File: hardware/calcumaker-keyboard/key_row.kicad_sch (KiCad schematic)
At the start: 30 parts, among them SW1 MX, SW10 MX, SW2 MX, SW3 MX, SW4 MX, SW5 MX, SW6 MX, SW7 MX, SW8 MX, SW9 MX

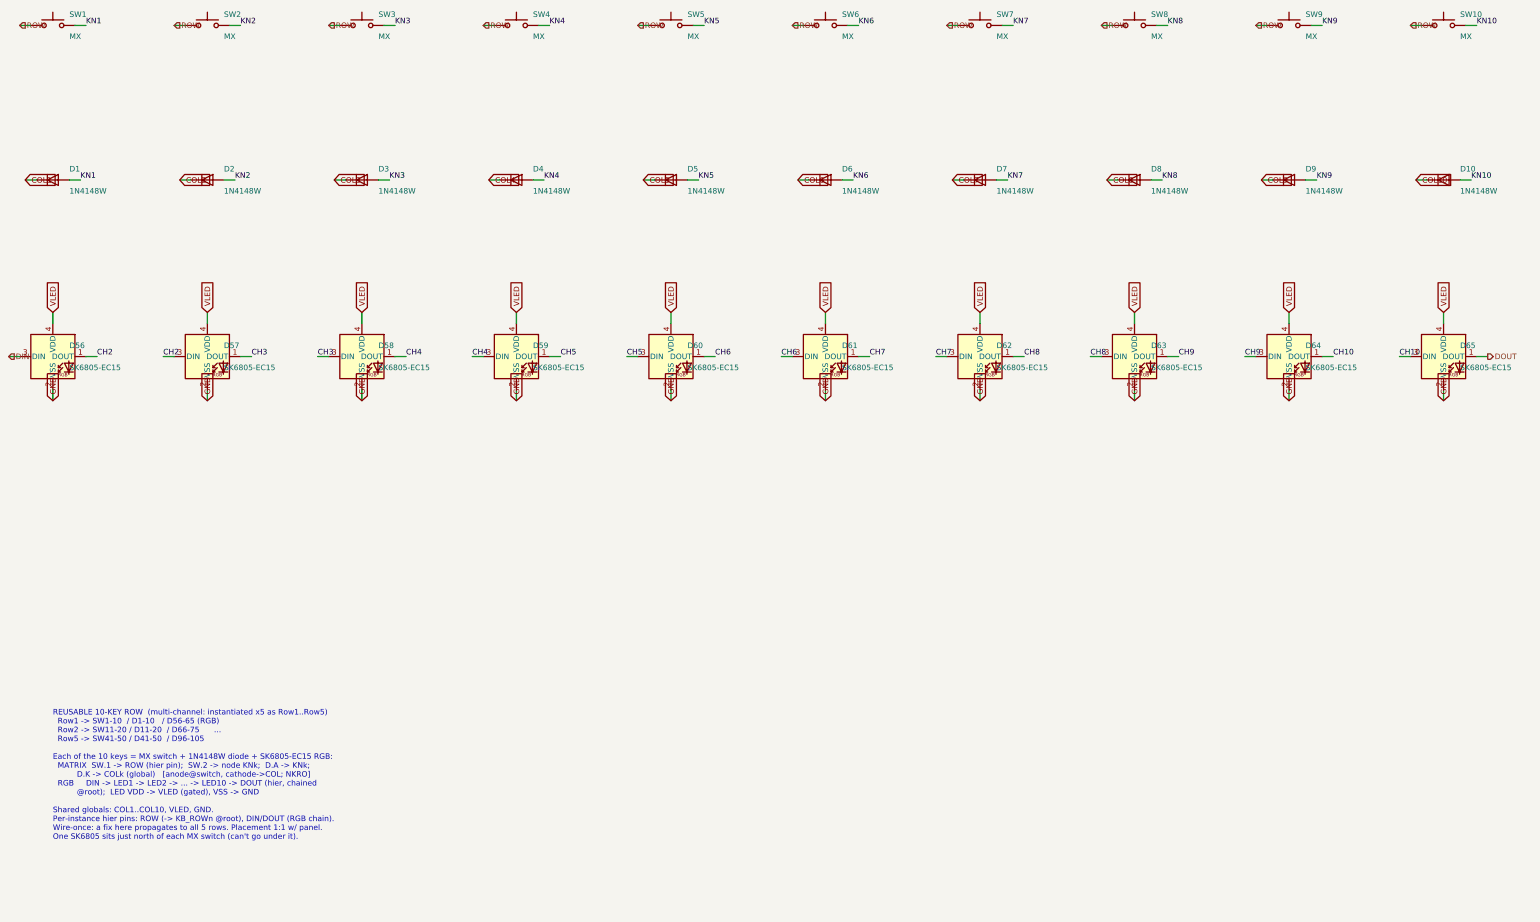
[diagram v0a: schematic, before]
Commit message: hardware: keyswitch 3D models, hot-swap footprint, reverse-mount per-key RGB
Physical build-out of the keyboard: real switch 3D, a hot-swap footprint, and a
single-sided-assembly LED choice.

- 3D models (vendored, hardware/lib/3dmodels): SW_Cherry_MX_1.00u_PCB.step from
  kiswitch/kiswitch (MIT) -- KiCad's Button_Switch_Keyboard.3dshapes does not
  exist in packages3D upstream, so there's nothing to install/download from
  KiCad -- plus HS_CPG151101S11_MX.step (socket) from marbastlib (CERN-OHL-P).
  Also vendor a plain solder-in SW_Cherry_MX_1.00u_PCB.kicad_mod (fallback).

- Keyswitch footprint -> marbastlib SW_MX_HS_CPG151101S11_1u (CERN-OHL-P): the
  Kailh CPG151101S11 hot-swap socket (LCSC C41430893). PLACE-ON-BACK -- switch
  fps go on the board's back copper layer so the socket (authored on F.Cu) lands
  on the physical bottom. HOT-SWAP ONLY: the switch thru-holes are 0.15mm-ring
  socket pass-throughs, NOT solder pads, so a switch-only/solder-in build would
  be a separate board rev (using the vendored solder-in-only fp). The switch-body
  (model) is on the footprint's B side so it renders opposite the socket for
  place-on-back. (Corrects an earlier, wrong "one-board solder+hotswap combo"
  framing -- the pass-throughs don't make a reliable solder joint.)

- Per-key RGB SK6805-EC15 -> SK6812MINI-E (LCSC C5149201), reverse/bottom mount
  (KiCad LED_SK6812MINI-E_3.2x2.8mm_P1.5mm_ReverseMount fp + bundled 3D): the LED
  sits on the bottom with the sockets -> SINGLE-SIDED assembly (one stencil, no
  flip), shining up through the switch's north LED window. Uses the base
  LED:SK6812 symbol (MINI-E `extends` it; kschgen doesn't resolve extends) with
  value/fp/lcsc overridden.

- Docs: DESIGN.md ("Hot-swap switches (place-on-back)" + reverse-mount RGB),
  PARTS.md, both hardware/lib READMEs (with license attribution), memory.

All three boards regenerate + pass the structure check (mcu 55 / keyboard 178 /
display 60, no duplicate refs).

Co-Authored-By: Claude O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
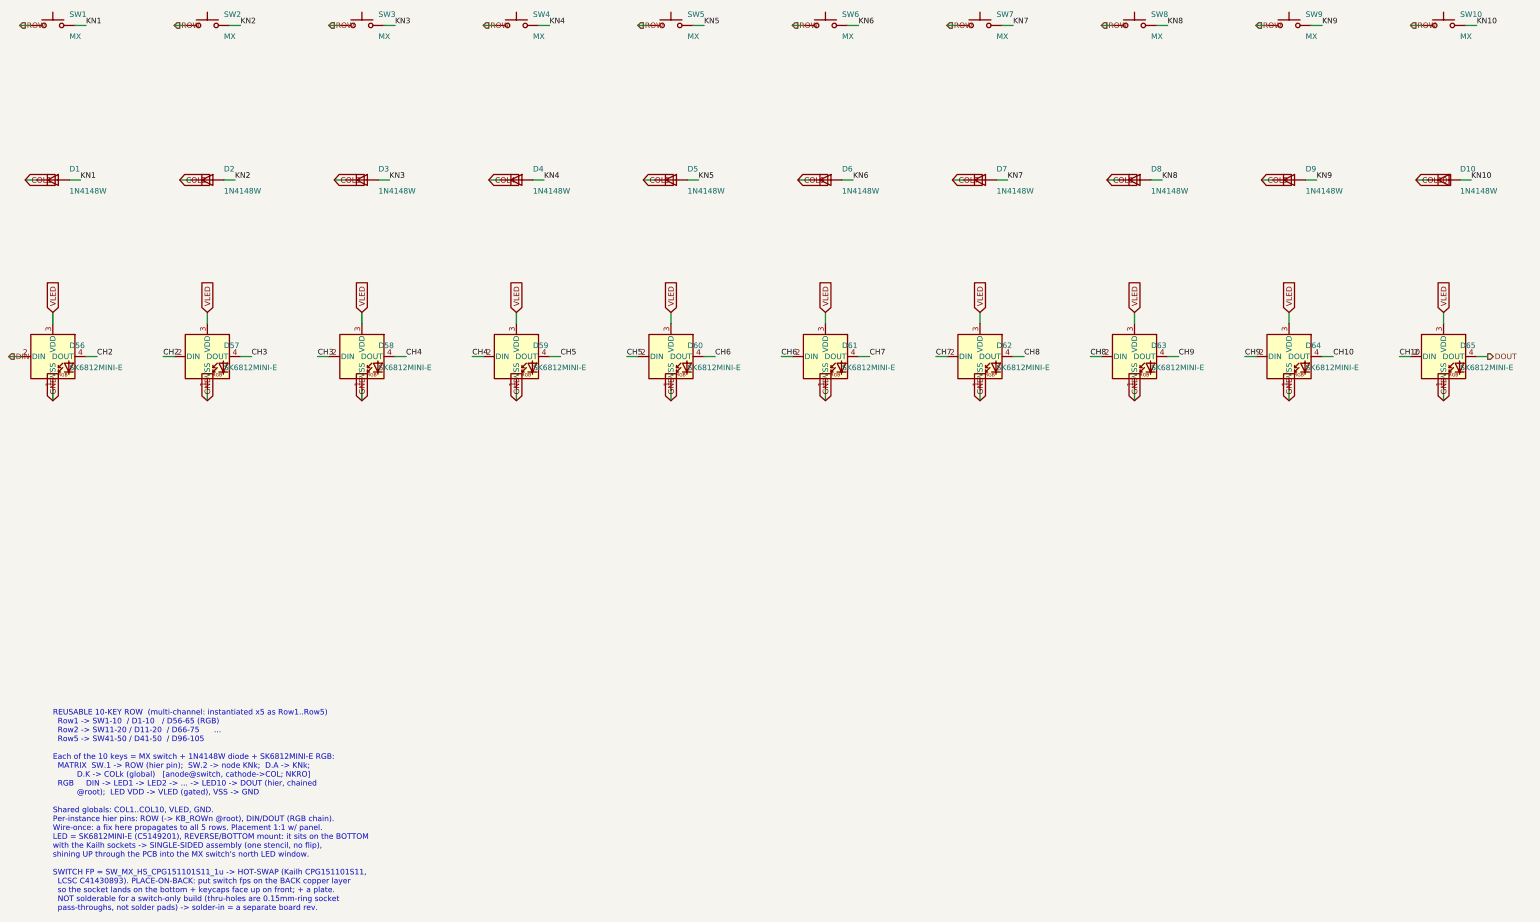
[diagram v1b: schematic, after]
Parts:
- removed D56, D57, D58, D59, D60, D61, D62, D63, D64, D65: SK6805-EC15, LED_SMD:LED_SK6812_EC15_1.5x1.5mm, symbol LED:SK6805
- added D56, D57, D58, D59, D60, D61, D62, D63, D64, D65: SK6812MINI-E, LED_SMD:LED_SK6812MINI-E_3.2x2.8mm_P1.5mm_ReverseMount, symbol LED:SK6812
- SW1, SW10, SW2, SW3, SW4, SW5, SW6, SW7, SW8, SW9: footprint Button_Switch_Keyboard:SW_Cherry_MX_1.00u_PCB -> calcumaker:SW_MX_HS_CPG151101S11_1u
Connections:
- net CH10: now also D64.4 (DOUT), D65.2 (DIN)
- net CH2: now also D56.4 (DOUT), D57.2 (DIN)
- net CH3: now also D57.4 (DOUT), D58.2 (DIN)
- net CH4: now also D58.4 (DOUT), D59.2 (DIN)
- net CH5: now also D59.4 (DOUT), D60.2 (DIN)
- net CH6: now also D60.4 (DOUT), D61.2 (DIN)
- net CH7: now also D61.4 (DOUT), D62.2 (DIN)
- net CH8: now also D62.4 (DOUT), D63.2 (DIN)
- net CH9: now also D63.4 (DOUT), D64.2 (DIN)
- net DIN: now also D56.2 (DIN)
- net DOUT: now also D65.4 (DOUT)
- net GND: now also D56.1 (VSS), D57.1 (VSS), D58.1 (VSS), D59.1 (VSS), D60.1 (VSS), D61.1 (VSS), D62.1 (VSS), D63.1 (VSS), D64.1 (VSS), D65.1 (VSS)
- net VLED: now also D56.3 (VDD), D57.3 (VDD), D58.3 (VDD), D59.3 (VDD), D60.3 (VDD), D61.3 (VDD), D62.3 (VDD), D63.3 (VDD), D64.3 (VDD), D65.3 (VDD)
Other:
- note added: "REUSABLE 10-KEY ROW (multi-channel: instantiated x5 as Row1..Row5) Row1 -> SW1-10 / D1-10 / D56-65 (RGB) Row2 -> SW11-20 / D11-20 / D66-75 ... Row5 -> SW41-50 / D41-50 / D96-105 Each of the 10 keys = MX switch + 1N4148W diode + SK6812MINI-E RGB: MATRIX SW.1 -> ROW (hier pin); SW.2 -> node KNk; D.A -> KNk; D.K -> COLk (global) [anode@switch, cathode->COL; NKRO] RGB DIN -> LED1 -> LED2 -> ... -> LE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"
- note removed: "REUSABLE 10-KEY ROW (multi-channel: instantiated x5 as Row1..Row5) Row1 -> SW1-10 / D1-10 / D56-65 (RGB) Row2 -> SW11-20 / D11-20 / D66-75 ... Row5 -> SW41-50 / D41-50 / D96-105 Each of the 10 keys = MX switch + 1N4148W diode + SK6805-EC15 RGB: MATRIX SW.1 -> ROW (hier pin); SW.2 -> node KNk; D.A -> KNk; D.K -> COLk (global) [anode@switch, cathode->COL; NKRO] RGB DIN -> LED1 -> LED2 -> ... -> LED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"
- title: Calcumaker 16 — Keyboard — Reusable 10-key row (MX + diode + SK6805 RGB) -> Calcumaker 16 — Keyboard — Reusable 10-key row (MX + diode + SK6812MINI-E RGB)
